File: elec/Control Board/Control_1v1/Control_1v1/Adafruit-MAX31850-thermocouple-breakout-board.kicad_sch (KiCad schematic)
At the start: 34 parts, among them J2 MAX31850K

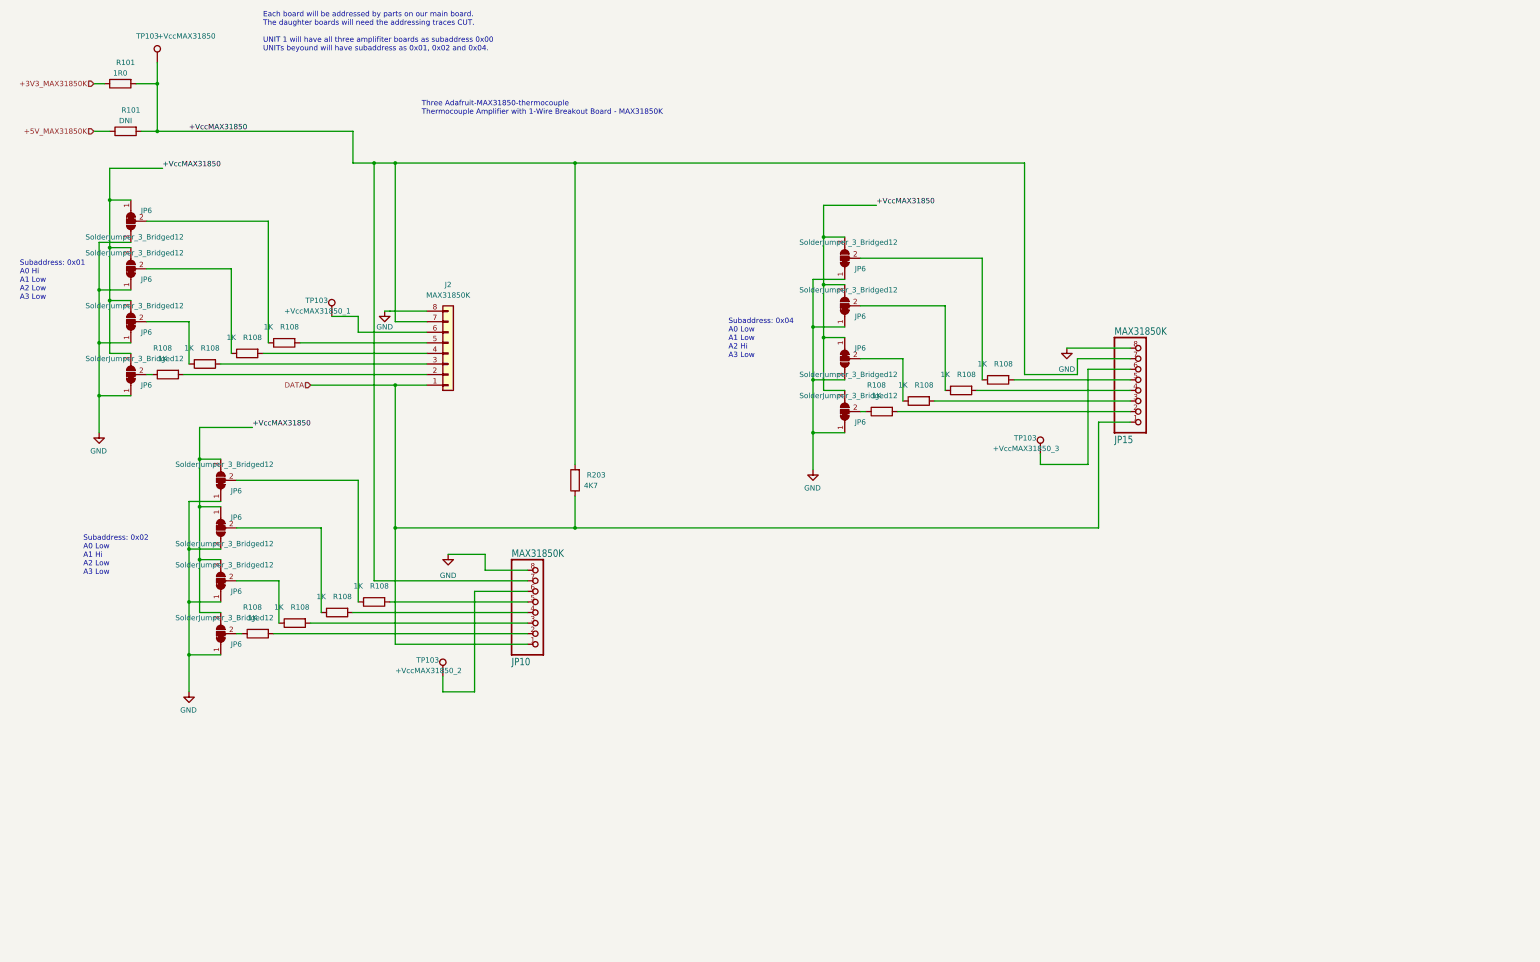
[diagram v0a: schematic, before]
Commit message: Add sheet with title block.
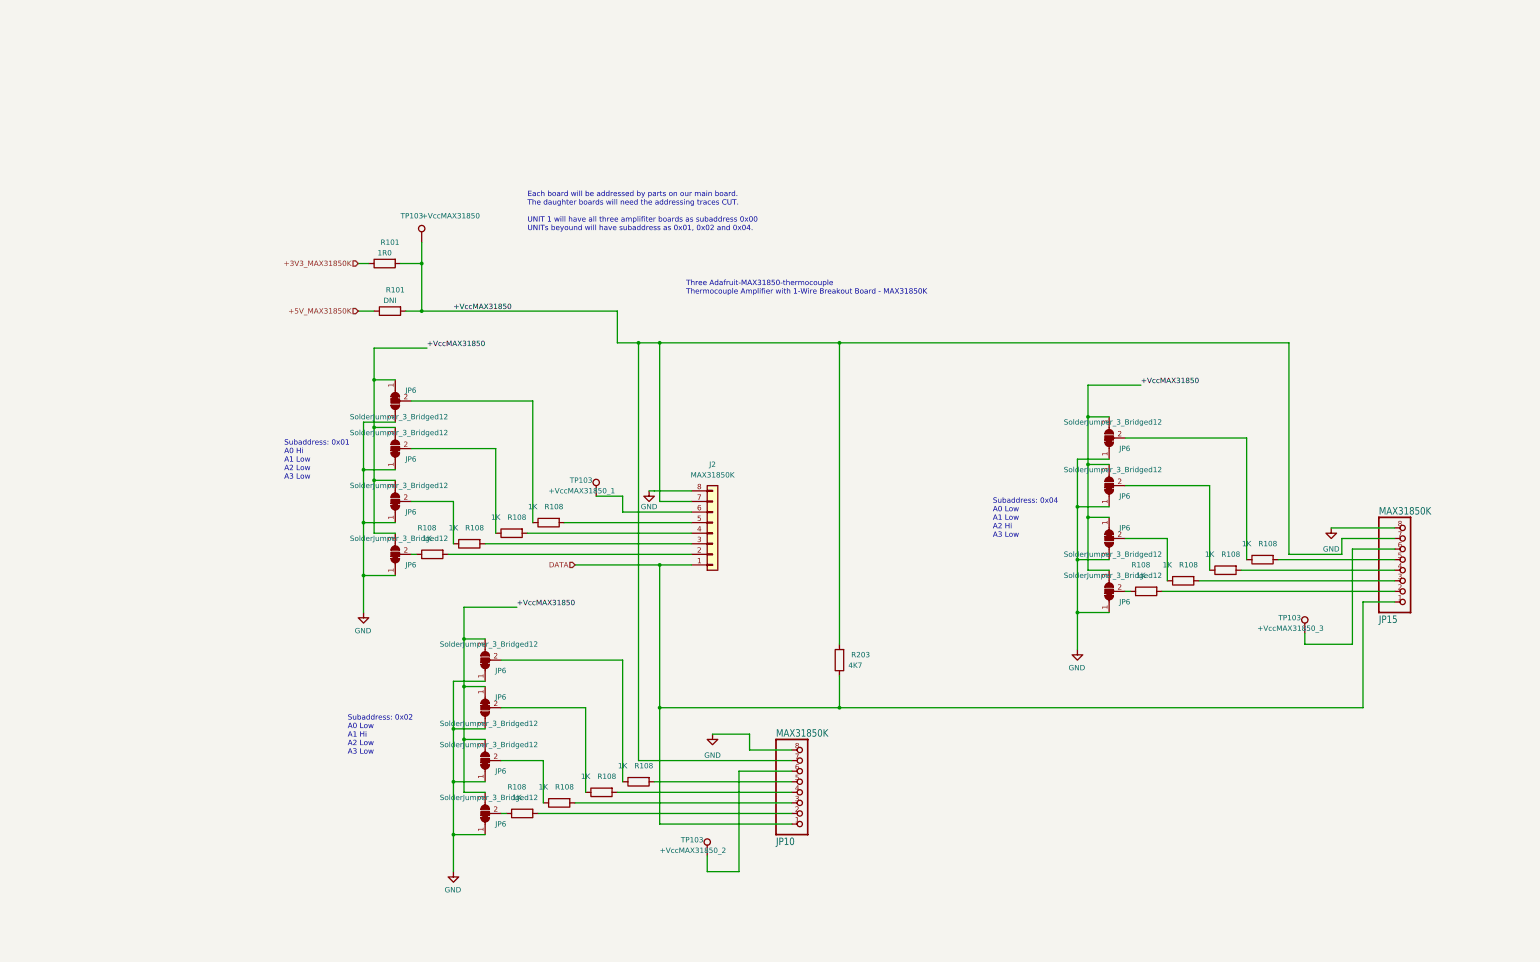
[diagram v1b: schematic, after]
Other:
- company: (none) -> Public Invention
- title: (none) -> Control Interconnect Board
- moved on the sheet: J2, JP10, JP15, JP6, R101, R108, R203, TP103

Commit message: Fix J10 backwards.
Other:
- title: Control Interconnect Board -> Control Interconnect Board OEDCS
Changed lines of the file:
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@@
   (paper "USLedger")
   (title_block
-    (title "Control Interconnect Board")
+    (title "Control Interconnect Board OEDCS")
     (date "2023-10-10")
     (rev "Rev 1.1")
     (company "Public Invention")
-    (comment 1 "Contributor: Lawrence Kinceloe")
+    (comment 1 "GNU Affero General Public License v3.0")
+    (comment 2 "Contributor: Lawrence Kinceloe")
+    (comment 3 "Drawn By: (Forrest) Lee Erickson")
   )
   (junction (at 266.7 120.65) (diameter 0) (color 0 0 0 0)

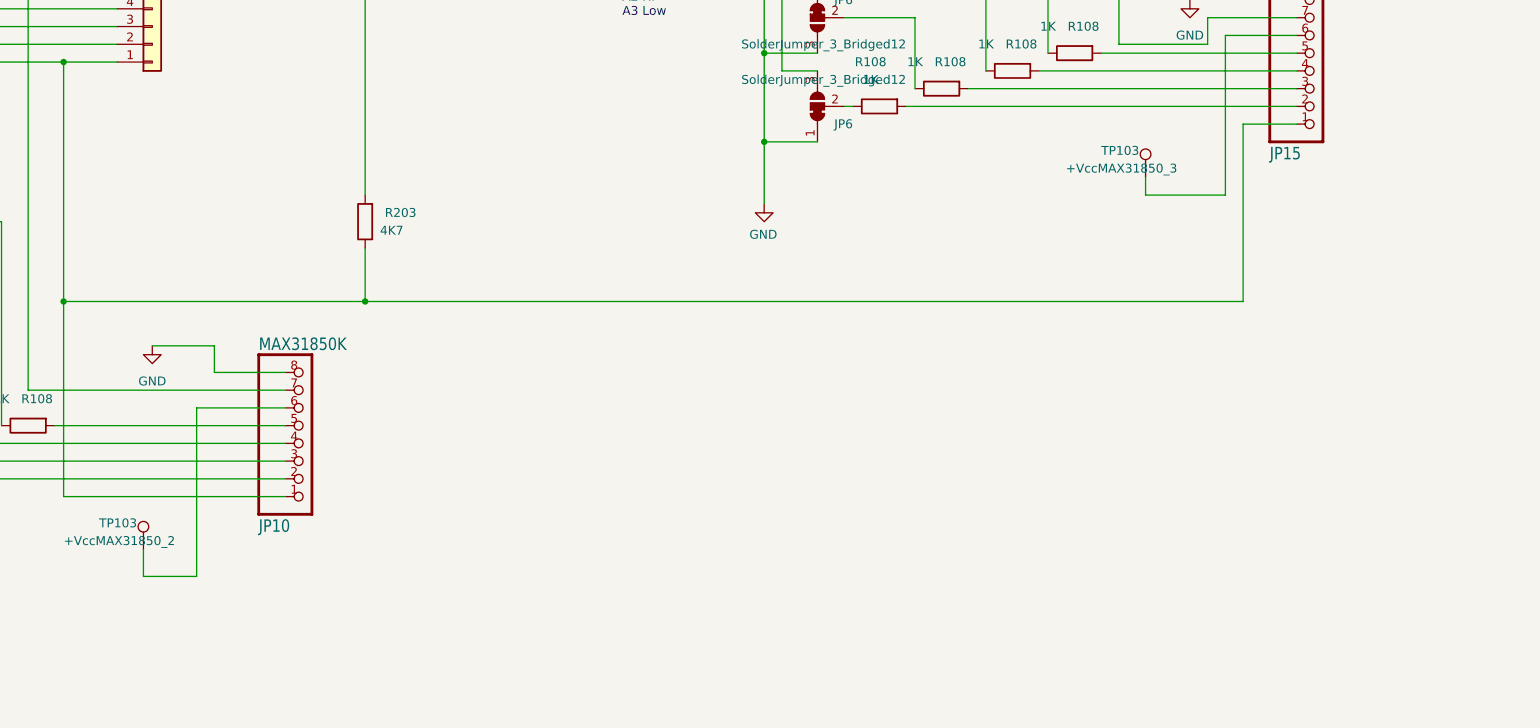
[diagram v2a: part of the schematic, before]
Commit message: Add power shutdown button. Add thermocouple ground screw terminals. Isolate SCL from SDA traces. Make first cut BOM.
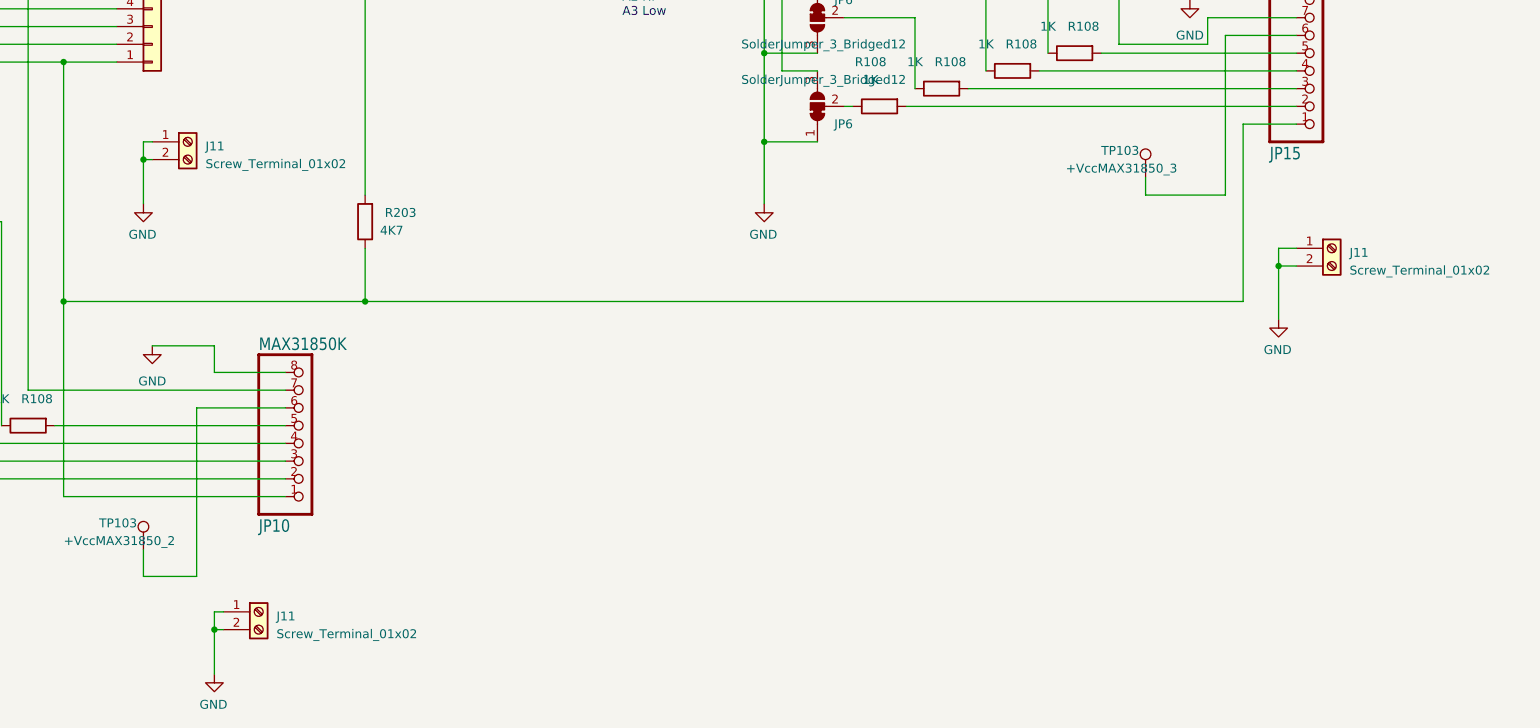
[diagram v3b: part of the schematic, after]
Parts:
- added J11 (x3): Screw_Terminal_01x02, TerminalBlock_TE-Connectivity:TerminalBlock_TE_282834-2_1x02_P2.54mm_Horizontal, symbol Connector:Screw_Terminal_01x02
- R101: LongLead (none) -> NO
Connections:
- net GND: now also J11.1 (Pin_1), J11.1 (Pin_1), J11.1 (Pin_1), J11.2 (Pin_2), J11.2 (Pin_2), J11.2 (Pin_2)
